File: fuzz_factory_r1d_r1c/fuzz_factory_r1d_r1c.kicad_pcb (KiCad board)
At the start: 2 copper layers, 109.2 x 114.3 mm, 42 parts, among them X1 +, X2 -, X3 COM

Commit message: Fuzz Factory [MB:REV1D/PB:REV1C]: universal capacitor footprints implemented
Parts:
- C3, C5, C6: footprint KCL-TH-SL:CP-RADIAL-D05.0-P02.0-CLS -> SBKCL-TH-SL:C-DISK-D04.2-T03.0-P05.08-d0.5-OR-CP-RADIAL-D05.0-P02.0-CLS
- moved C5 1.27 mm to (127.0, 133.3)
- moved C6 1.27 mm to (175.3, 90.2)
- moved C3 1.27 mm to (167.6, 133.3)
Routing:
- net Net-(C3-Pad+): track 56.3 -> 57.8 mm
- net /IN-CON: track 38.6 -> 40.1 mm
- net /MB5: track 62.5 -> 63.6 mm

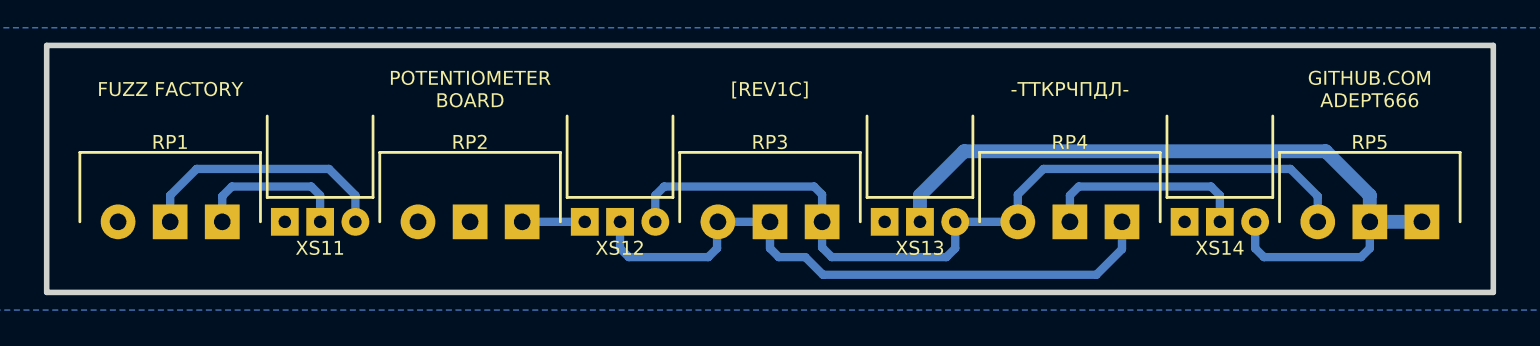
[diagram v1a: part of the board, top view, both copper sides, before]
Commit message: Fuzz Factory [MB:REV1D/PB:REV1C]: potentiometer board text objects flipped
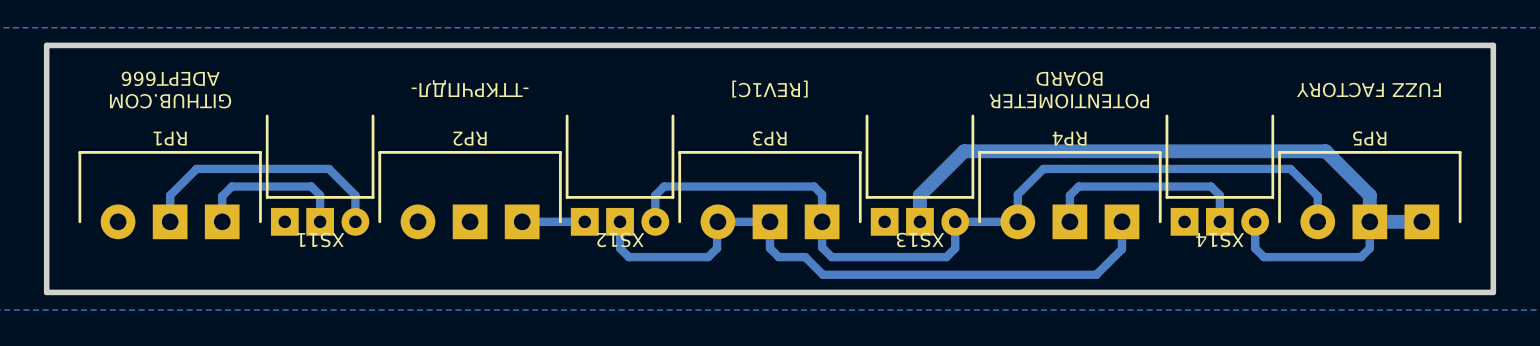
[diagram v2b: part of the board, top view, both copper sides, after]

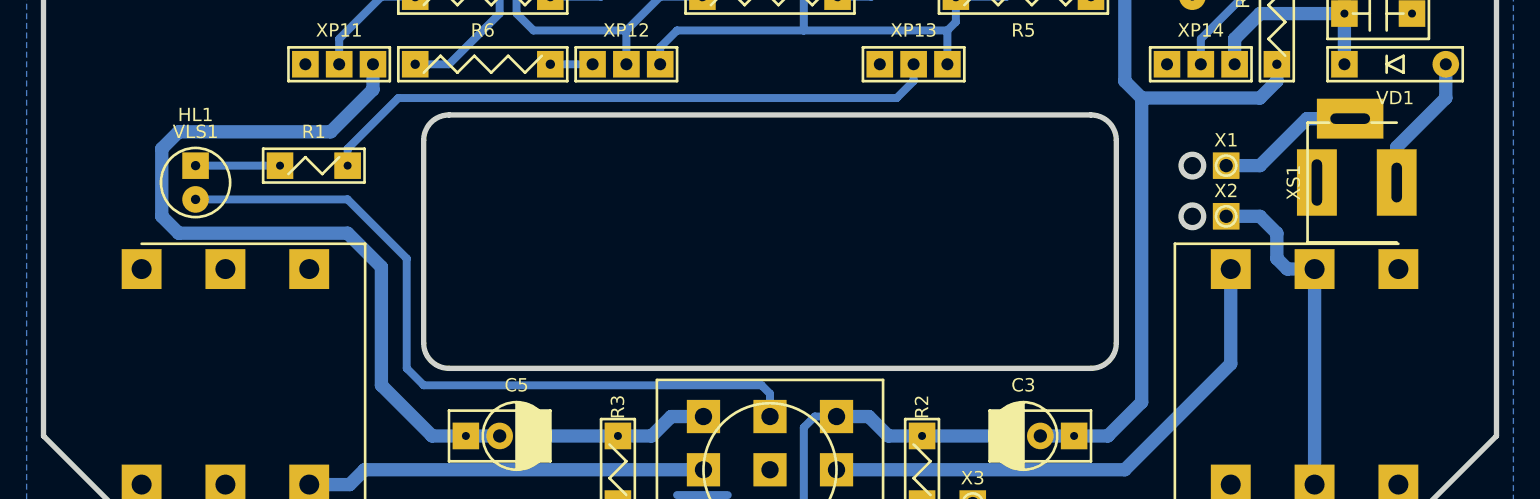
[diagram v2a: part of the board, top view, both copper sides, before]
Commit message: Fuzz Factory [MB:REV1D/PB:REV1C]: minor changes
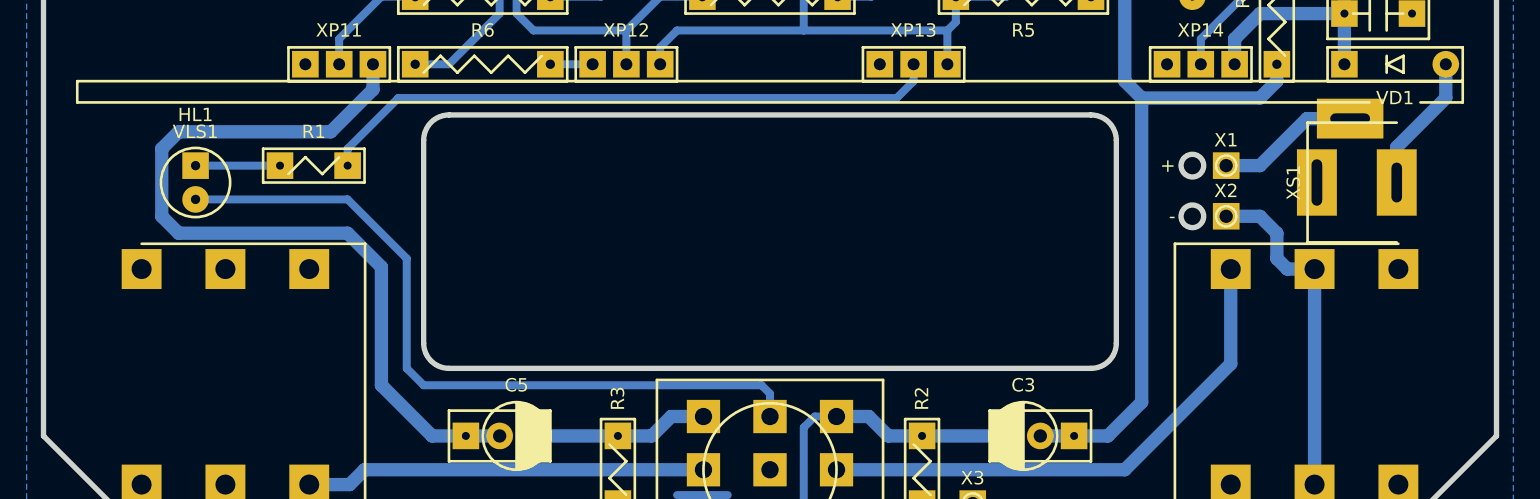
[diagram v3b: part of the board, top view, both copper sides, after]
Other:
- board text added: "+"
- board text added: "-"

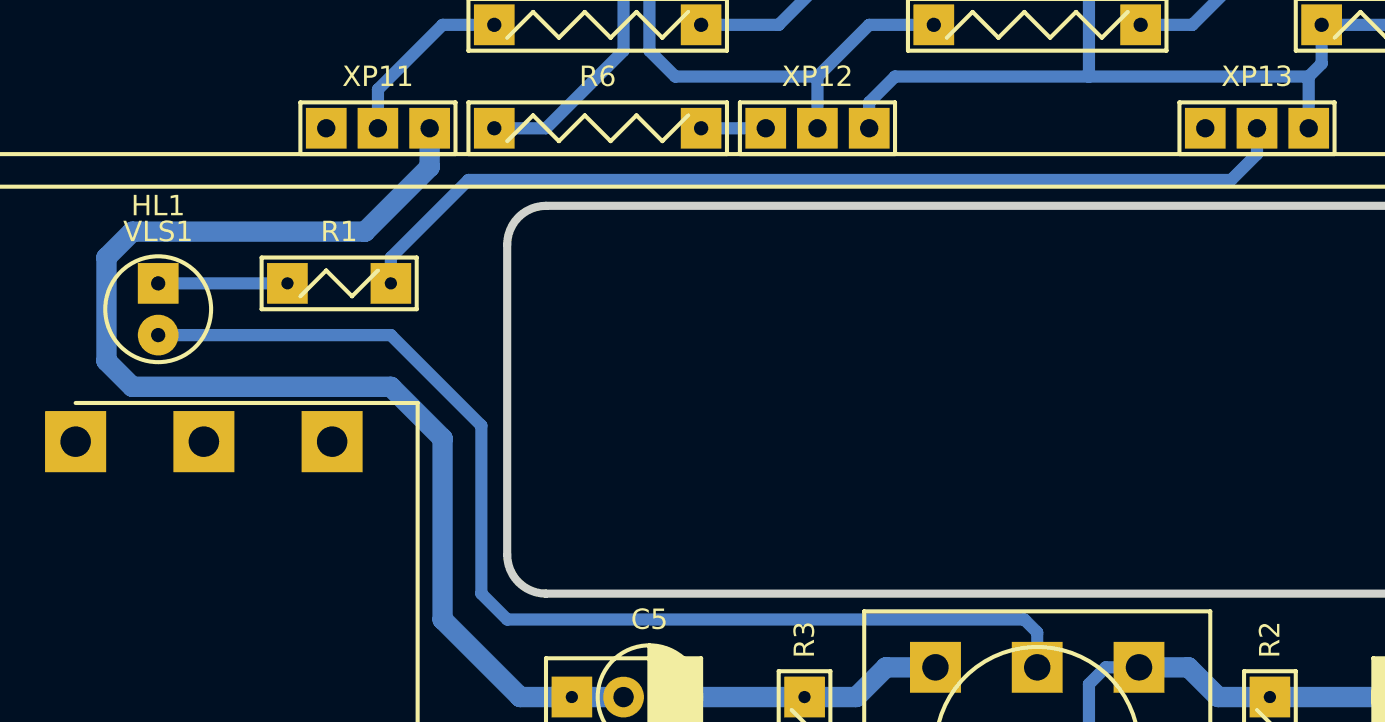
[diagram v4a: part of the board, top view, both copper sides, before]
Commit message: Fuzz Factory [MB:REV1D/PB:REV1C]: R9 added
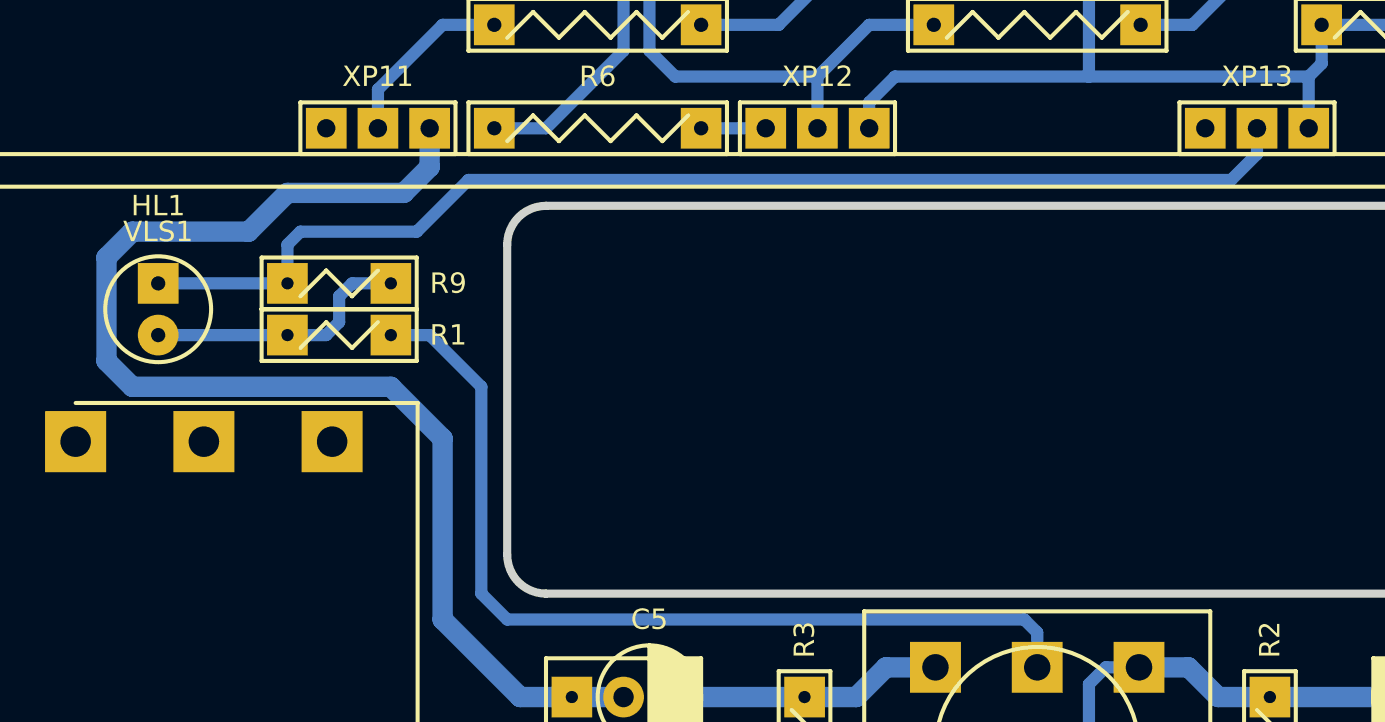
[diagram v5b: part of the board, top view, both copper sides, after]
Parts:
- added R9: 105, KCL-TH-SL:R-MFR-12, F.Cu at (113.0, 113.0)
- moved R1 2.54 mm to (113.0, 115.6), turned to 180 degrees
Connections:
- HL1 pad A: Net-(HL1-PadA) -> V
- HL1 pad C: /LED -> Net-(HL1-PadC)
- R1 pad 1: Net-(HL1-PadA) -> /LED
- R1 pad 2: V -> Net-(HL1-PadC)
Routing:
- net Net-(HL1-PadC): track 0.00 -> 13.2 mm
- net V: track 78.2 -> 90.0 mm
- net /LED: track 55.8 -> 45.5 mm
- net Net-(HL1-PadA): track 6.35 -> 0.00 mm

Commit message: Fuzz Factory [MB:REV1D/PB:REV1C]: minor changes
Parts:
- R9: value 105 -> X
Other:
- board text added: "1. R9 не устанавливать."
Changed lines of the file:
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@@
   (general
     (thickness 1.6)
-    (drawings 45)
+    (drawings 46)
     (tracks 204)
     (zones 0)
@@
   (title_block
     (title "Fuzz Factory")
-    (date 2022-01-09)
+    (date 2022-02-20)
     (rev MB:1D/PB:1C)
     (company "Igor Ivanov")
@@
       (effects (font (size 1 1) (thickness 0.2)) (justify left))
     )
-    (fp_text value 105 (at 0 0 180) (layer F.Fab)
+    (fp_text value X (at 0 0 180) (layer F.Fab)
       (effects (font (size 1 1) (thickness 0.2)))
     )
@@
     (fp_arc (start -52.25 27.1) (end -49 27.1) (angle -90) (layer Eco1.User) (width 0.4))
     (fp_arc (start 52.25 27.1) (end 52.25 23.85) (angle -90) (layer Eco1.User) (width 0.4))
+  )
+  (gr_text "1. R9 не устанавливать." (at 176.53 162.56) (layer F.Fab)
+    (effects (font (size 2.54 2.54) (thickness 0.2)) (justify left))
   )
   (gr_line (start 196.215 108.28) (end 199.39 108.28) (layer F.SilkS) (width 0.2))
@@
   (segment (start 194.43 111.64) (end 198.12 107.95) (width 1) (layer B.Cu) (net 8))
   (segment (start 198.12 107.95) (end 198.12 105.41) (width 1) (layer B.Cu) (net 8))
-  (segment (start 104.14 115.57) (end 110.49 115.57) (width 0.6) (layer B.Cu) (net 33))
   (segment (start 179.07 97.79) (end 176.53 97.79) (width 1) (layer B.Cu) (net 9))
   (segment (start 176.53 97.79) (end 173.99 100.33) (width 1) (layer B.Cu) (net 9))
@@
   (segment (start 138.43 133.35) (end 135.89 133.35) (width 1) (layer B.Cu) (net 32))
   (segment (start 135.89 133.35) (end 129.54 133.35) (width 1) (layer B.Cu) (net 32))
+  (segment (start 104.14 115.57) (end 110.49 115.57) (width 0.6) (layer B.Cu) (net 33))
   (segment (start 112.395 115.57) (end 113.03 114.935) (width 0.6) (layer B.Cu) (net 33))
   (segment (start 110.49 115.57) (end 112.395 115.57) (width 0.6) (layer B.Cu) (net 33))
